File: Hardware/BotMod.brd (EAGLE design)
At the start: 80 x 31 mm, 42 parts, among them Q1 BSS138, Q2 BSS138, T1 MMBT2222A, U1 LSM303D

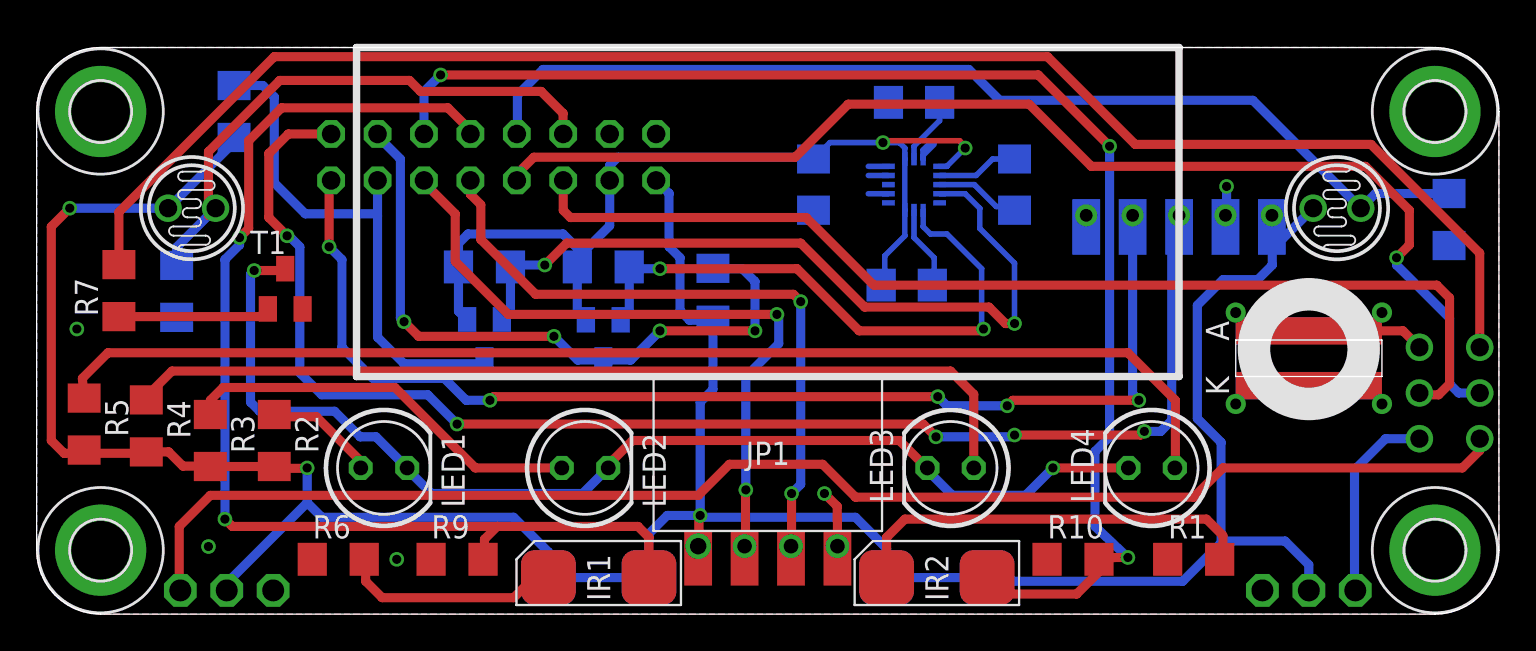
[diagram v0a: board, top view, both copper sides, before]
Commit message: Redesigned BotMod (R2) with support for:  - ToF distance sensors VL6180X (5-100mm) and VL53L1X (40-4000mm)  - SMD High Intensity Led
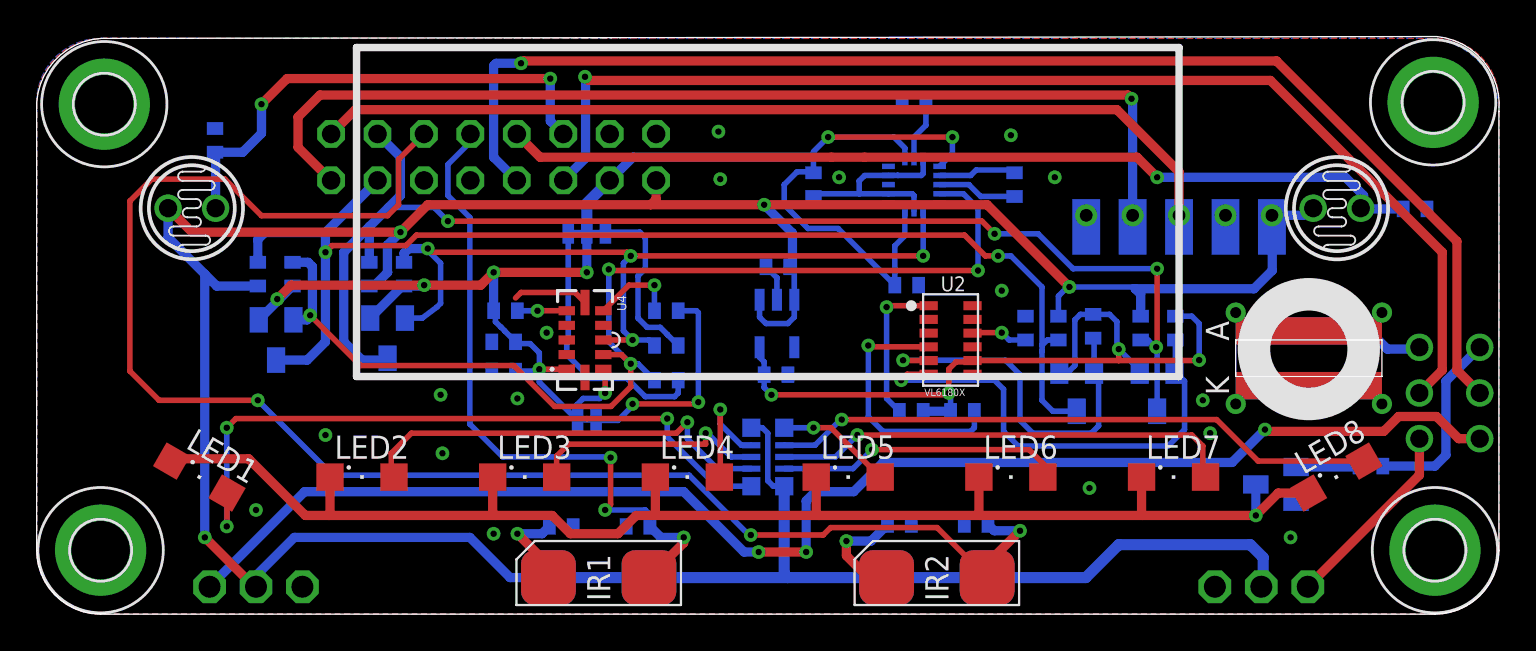
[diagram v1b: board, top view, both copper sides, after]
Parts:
- removed JP1: (no value), SpaceDIY_connectors:PINHEAD_4_FEMALE
- added AR1: 150, SpaceDIY:RESISTOR_ARRAY_X8_CAY17
- added C5, C6, C7: 10uF, Passive_components:0402
- added C8: 0.1uF, Passive_components:0402
- added C9: 4.7uF, Passive_components:0402
- added I2C: (no value), SparkFun-Jumpers:SMT-JUMPER_3_2-NC_TRACE_SILK
- added JP9: INT, SparkFun-Passives:PAD-JUMPER-2-NC_BY_TRACE_YES_SILK
- added LED5, LED6, LED7, LED8: (no value), led:SML1206
- added Q3, Q4: BSS138, adafruit:SOT23
- added R16, R17, R18, R19: 10k, Passive_components:0402
- added R20, R21: 2.2k, Passive_components:0402
- added U2: VL6180X, microbuilder:VL6180
- added U3: MIC5225_2.8V, microbuilder:SOT23-5
- added U4: VL53L1X, SparkFun-Sensors:VL53L1X
- C1, C2, C3, C4: device resistor:C1206 -> Passive_components:0402
- LED1, LED2, LED3, LED4: device led:LED5MM -> led:SML1206
- R1, R10, R11, R12, R13, R14, R15, R6, R7, R8, R9: device resistor:R1206 -> Passive_components:0402
- R2, R3: value 200 -> 47k; device resistor:R1206 -> Passive_components:0402
- R4, R5: value 200 -> 10k; device resistor:R1206 -> Passive_components:0402
- moved R7 69.2 mm to (73.0, 8.10), flipped to the bottom, turned to 180 degrees
- moved T1 55.2 mm to (67.8, 7.10), flipped to the bottom, turned to 270 degrees
- moved R3 41.2 mm to (50.6, 11.1), flipped to the bottom, turned to 0 degrees
- moved R2 34.9 mm to (47.9, 11.1), flipped to the bottom, turned to 180 degrees
- moved R5 32.4 mm to (34.5, 16.6), flipped to the bottom, turned to 180 degrees
- moved LED4 25.4 mm to (35.6, 7.50), turned to 0 degrees
- moved LED3 23.3 mm to (26.7, 7.50), turned to 0 degrees
- moved R4 20.6 mm to (25.6, 16.6), flipped to the bottom, turned to 0 degrees
- moved R14 18.8 mm to (18.2, 18.6)
- moved R1 16.2 mm to (47.2, 4.90), flipped to the bottom
- moved R6 12.3 mm to (28.7, 4.80), flipped to the bottom
- moved LED2 12.2 mm to (17.8, 7.50)
- moved Q2 11.8 mm to (19.2, 15.1)
- moved Q1 11.4 mm to (13.1, 15.0)
- moved R13 10.9 mm to (20.1, 18.6), turned to 270 degrees
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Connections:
- new net 2.8V: C6.1, Q3.1, Q4.1, R16.2, R18.2, R2.2, R3.2, U2.8, U3.5
- new net L1: AR1.1, LED1.A
- new net L2: AR1.2, LED2.A
- new net L3: AR1.3, LED3.A
- new net L4: AR1.4, LED4.A
- new net L5: AR1.6, LED5.A
- new net L6: AR1.7, LED8.A
- new net L7: AR1.8, LED7.A
- new net L8: AR1.9, LED6.A
- new net N$14: JP9.2, R5.2
- new net N$16: R4.1, U4.5
- new net N$19: R5.1, U4.7
- new net N$9: I2C.1, R21.2
- new net SCL2.8: Q3.2, R16.1, U2.5
- new net SDA2.8: Q4.2, R18.1, U2.6
- net 3.3V: now also C8.1, C9.1, I2C.2, JP9.1, R4.2, U4.1, U4.11
- net D2: now also Q4.3, R19.1
- net D3: now also Q3.3, R17.1
- net D7: no longer JP1.P$3
- net D8: no longer JP1.P$2
- net GND: now also C5.2, C6.2, C7.2, C8.2, C9.2, U2.12, U2.9, U3.2, U4.12, U4.2, U4.3, U4.4, U4.6; no longer JP1.P$4
- net N$1: now also LED1.C, LED2.C, LED3.C, LED4.C, LED5.C, LED6.C, LED7.C, LED8.C; no longer LED1.K, LED2.K, LED3.K, LED4.K
- net N$5: now also U2.1; no longer LED1.A
- net N$6: now also U2.4; no longer LED2.A
- net N$7: now also I2C.3, R20.2; no longer LED3.A, R4.1
- net N$8: now also C7.1, U2.10; no longer LED4.A, R5.1
- net SCL: now also R21.1, U4.10
- net SDA: now also R20.1, U4.9
- net VCC: now also AR1.10, AR1.5, C5.1, R17.2, R19.2, U3.1, U3.3; no longer JP1.P$1, R2.2, R3.2, R4.2, R5.2
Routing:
- net LED: track 90.5 -> 10.4 mm
- net N$8: track 66.3 -> 3.08 mm, vias 0 -> 1
- net 2.8V: track 0.00 -> 43.7 mm, vias 0 -> 4
- net N$7: track 50.6 -> 9.70 mm
- net D8: track 40.1 -> 0.00 mm, vias 2 -> 0
- net D3: track 28.7 -> 68.4 mm, vias 0 -> 2
- net D7: track 38.4 -> 0.00 mm, vias 2 -> 0
- net L1: track 0.00 -> 38.3 mm, vias 0 -> 3
- net 3.3V: track 52.8 -> 89.8 mm, vias 2 -> 8
- net D2: track 36.9 -> 70.4 mm
- net L6: track 0.00 -> 33.2 mm, vias 0 -> 1
- net D0: track 77.4 -> 50.7 mm, vias 5 -> 0
- net A3: track 62.8 -> 36.7 mm, vias 2 -> 3
- net SDA2.8: track 0.00 -> 25.5 mm, vias 0 -> 1
- net L7: track 0.00 -> 25.4 mm, vias 0 -> 1
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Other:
- board size 80 x 31 mm -> 80 x 31.6 mm

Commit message: Updated LED Resistors
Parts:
- removed AR1: 150, SpaceDIY:RESISTOR_ARRAY_X8_CAY17
- removed JP4: (no value), pinhead:1X03
- added JP1: (no value), SpaceDIY_connectors:PINHEAD_5_FEMALE
- added U$1, U$2, U$3, U$4, U$5, U$6, U$7, U$8: R1206, Passive_components:1206
- JP2: device SpaceDIY_connectors:PINHEAD_5_FEMALE -> pinhead:1X03
- R2: value 47k -> 200
- R3: value 47k -> 1k
- R4, R5: value 10k -> 47k
- R6: value 200 -> 10k
- R7: value 1k -> 10k
- U3: value MIC5225_2.8V -> VL53L1X; device microbuilder:SOT23-5 -> SparkFun-Sensors:VL53L1X
- U4: value VL53L1X -> MIC5225_2.8V; device SparkFun-Sensors:VL53L1X -> microbuilder:SOT23-5
- moved JP3 55.0 mm to (12.0, 1.50), turned to 180 degrees
- moved R7 48.1 mm to (25.6, 16.6), turned to 0 degrees
- moved JP2 25.8 mm to (67.0, 1.50)
- moved R4 25.6 mm to (50.6, 11.1)
- moved R3 22.6 mm to (73.0, 8.10), turned to 180 degrees
- moved R2 20.2 mm to (28.7, 4.80), turned to 0 degrees
- moved R5 14.5 mm to (47.9, 11.1)
- moved R6 13.1 mm to (34.5, 16.6), turned to 180 degrees
- moved U3 10.5 mm to (30.0, 15.0), flipped to the top, turned to 270 degrees
- moved U4 10.5 mm to (40.5, 15.9), flipped to the bottom, turned to 180 degrees
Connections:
- net 2.8V: now also R4.2, R5.2, U4.5; no longer R2.2, R3.2, U3.5
- net 3.3V: now also R7.2, U3.1, U3.11; no longer R4.2, U4.1, U4.11
- net D0: now also JP1.P$3; no longer JP2.P$3
- net D1: now also JP1.P$4; no longer JP2.P$4
- net GND: now also JP1.P$2, JP2.3, R2.1, U3.12, U3.3, U3.4, U3.6; no longer JP2.P$2, JP4.3, R6.1, U4.12, U4.3, U4.4, U4.6
- net L1: now also U$1.1; no longer AR1.1
- net L2: now also U$2.1; no longer AR1.2
- net L3: now also U$3.1; no longer AR1.3
- net L4: now also U$4.1; no longer AR1.4
- net L5: now also U$5.1; no longer AR1.6
- net L6: now also U$8.1; no longer AR1.7
- net L7: now also U$7.1; no longer AR1.8
- net L8: now also U$6.1; no longer AR1.9
- net LED: now also R3.2; no longer R7.2
- net N$14: now also R6.2; no longer R5.2
- net N$16: now also R7.1, U3.5; no longer R4.1, U4.5
- net N$19: now also R6.1, U3.7; no longer R5.1, U4.7
- net N$2: now also R3.1; no longer R7.1
- net N$3: now also R2.2; no longer R6.2
- net N$5: now also R5.1; no longer R2.1
- net N$6: now also R4.1; no longer R3.1
- net S1: now also JP3.1; no longer JP4.1
- net S2: now also JP2.1; no longer JP3.1
- net SCL: now also U3.10; no longer U4.10
- net SDA: now also U3.9; no longer U4.9
- net VCC: now also JP1.P$1, JP2.2, U$1.2, U$2.2, U$3.2, U$4.2, U$5.2, U$6.2, U$7.2, U$8.2, U4.1, U4.3; no longer AR1.10, AR1.5, JP2.P$1, JP4.2, U3.1, U3.3
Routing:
- net L1: track 38.3 -> 8.27 mm, vias 3 -> 1
- net L6: track 33.2 -> 14.5 mm
- net L7: track 25.4 -> 7.56 mm
- net L2: track 23.3 -> 5.80 mm
- net VCC: track 185.3 -> 174.2 mm
- net L4: track 6.70 -> 17.6 mm
- net L8: track 15.7 -> 6.39 mm
- net L5: track 6.37 -> 10.2 mm
- net L3: track 13.2 -> 9.56 mm
- net N$1: track 79.4 -> 77.5 mm
- net GND: vias 17 -> 18

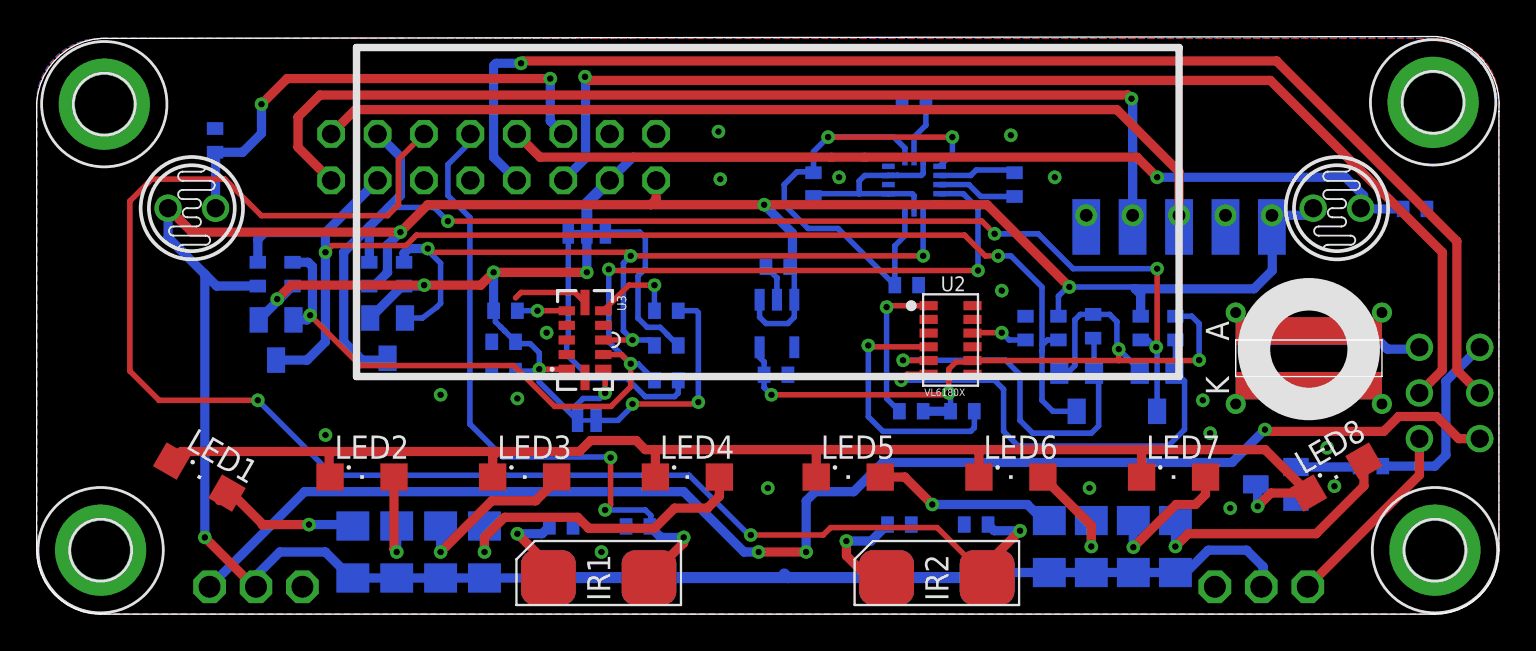
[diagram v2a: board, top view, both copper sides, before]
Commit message: Replaced LED lights with 7310 package
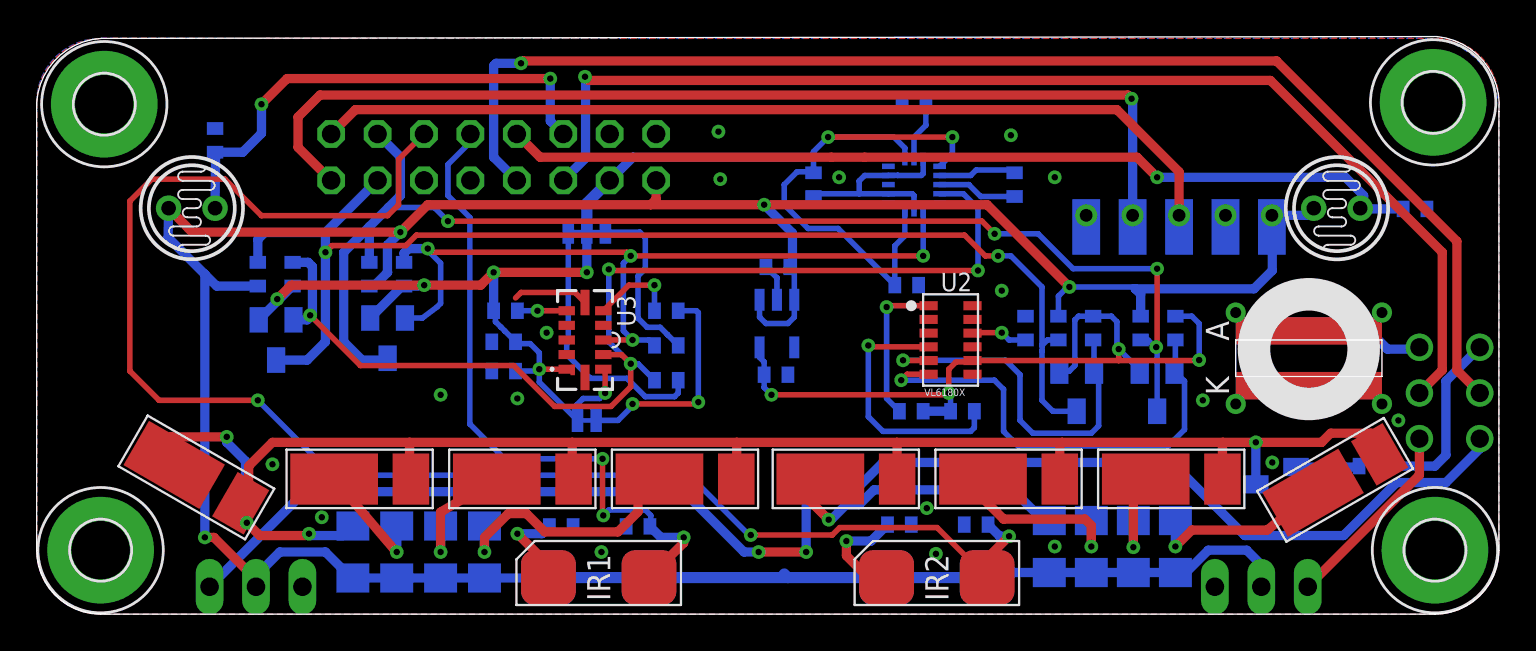
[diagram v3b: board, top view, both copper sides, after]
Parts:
- H1, H2, H3, H4: value (none) -> MOUNT-PAD-ROUND3.2
- LDR1, LDR2: value (none) -> VT20N1
- LED1, LED2, LED3, LED4, LED5, LED6, LED7, LED8: value (none) -> LED5730; device led:SML1206 -> SpaceDIY_passive_components:LED5730
- moved R16 0.10 mm to (57.8, 15.7)
- renumbered U$1 to R22, U$2 to R23, U$3 to R24, U$4 to R25, U$5 to R26, U$6 to R27, U$7 to R28, U$8 to R29
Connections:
- net L1: now also LED1.P$1; no longer LED1.A
- net L2: now also LED2.P$1; no longer LED2.A
- net L3: now also LED3.P$1; no longer LED3.A
- net L4: now also LED4.P$1; no longer LED4.A
- net L5: now also LED5.P$1; no longer LED5.A
- net L6: now also LED8.P$1; no longer LED8.A
- net L7: now also LED7.P$1; no longer LED7.A
- net L8: now also LED6.P$1; no longer LED6.A
- net N$1: now also LED1.P$2, LED2.P$2, LED3.P$2, LED4.P$2, LED5.P$2, LED6.P$2, LED7.P$2, LED8.P$2; no longer LED1.C, LED2.C, LED3.C, LED4.C, LED5.C, LED6.C, LED7.C, LED8.C
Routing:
- net L1: track 8.27 -> 16.2 mm, vias 1 -> 3
- net L5: track 10.2 -> 17.3 mm
- net L8: track 6.39 -> 11.7 mm
- net L6: track 14.5 -> 10.1 mm
- net N$1: track 77.5 -> 80.4 mm
- net L4: track 17.6 -> 14.9 mm
- net S1: track 78.3 -> 80.9 mm, vias 3 -> 2
- net L3: track 9.56 -> 7.17 mm
- net L7: track 7.56 -> 5.49 mm
- net A4: track 87.1 -> 86.1 mm
- net L2: track 5.80 -> 6.68 mm

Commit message: Updated Production files
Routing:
- net GND: track 17.8 -> 13.9 mm
- net L1: track 16.2 -> 15.3 mm, vias 3 -> 1
- net VCC: track 174.4 -> 175.2 mm
